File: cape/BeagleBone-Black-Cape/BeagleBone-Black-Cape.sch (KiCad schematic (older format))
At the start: 0 parts

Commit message: BBB cape rev-000
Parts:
- added J1, J2: USB_B, symbol USB_B
- added J3: Conn_01x03_Male, symbol Conn_01x03_Male
- added J4: Conn_01x02_Male, symbol Conn_01x02_Male
- added J5: Conn_01x05_Male, symbol Conn_01x05_Male
- added P8, P9: BeagleBone_Black_Header, symbol BeagleBone_Black_Header
- added U?: SN65HVD232, Housings_SOIC:SOIC-8_3.9x4.9mm_Pitch1.27mm, symbol SN65HVD232
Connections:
- new net +3V3: P9.3 (P3), P9.4 (P4), U?.3 (VCC)
- new net +5V: J1.1 (VBUS), J2.1 (VBUS), J3.3 (Pin_3), P9.5 (P5), P9.6 (P6)
- new net CANH: J4.1 (Pin_1), U?.7 (CANH)
- new net CANL: J4.2 (Pin_2), U?.6 (CANL)
- new net CAN_RX: U?.4 (R)
- new net CAN_TX: P9.24 (P24), U?.1 (D)
- new net GND: J1.4 (GND), J2.4 (GND), J3.1 (Pin_1), J5.5 (Pin_5), U?.2 (GND)
- new net GNDA_ADC: P9.34 (P34)
- new net GNDD: P8.1 (P1), P8.2 (P2), P9.1 (P1), P9.2 (P2), P9.43 (P43), P9.44 (P44), P9.45 (P45), P9.46 (P46)
- new net PWR_BUT: P9.9 (P9)
- new net SPI_MISO: J5.3 (Pin_3), P9.21 (P21)
- new net SPI_MOSI: J5.2 (Pin_2), P9.18 (P18)
- new net SPI_SCK: J5.4 (Pin_4), P9.22 (P22)
- new net SPI_SS: J5.1 (Pin_1), P9.17 (P17)
- new net SYS_5V: P9.7 (P7), P9.8 (P8)
- new net SYS_RESETN: P9.10 (P10)
- new net TACH_IN: J3.2 (Pin_2), P9.27 (P27)
- new net USB1+: J1.3 (D+), P8.15 (P15)
- new net USB1-: J1.2 (D-), P8.17 (P17)
- new net USB2+: J2.3 (D+), P8.16 (P16)
- new net USB2-: J2.2 (D-), P8.18 (P18)
- new net VDD_ADC: P9.32 (P32)
- no-connect marks 0 -> 2
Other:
- note added: "1. CANbus tranceiver has two sister chips that offer a \n offer "Standby" mode and "Sleep mode"\n2. Should we add any status LEDs for debug/functionality?\n3. Not sure if the shield option should be used for the USB.\n4. Bosch 928000453 for tachometer connection?\n"
- note added: "Notes:"
- note removed: "USB"
- note removed: "\n"

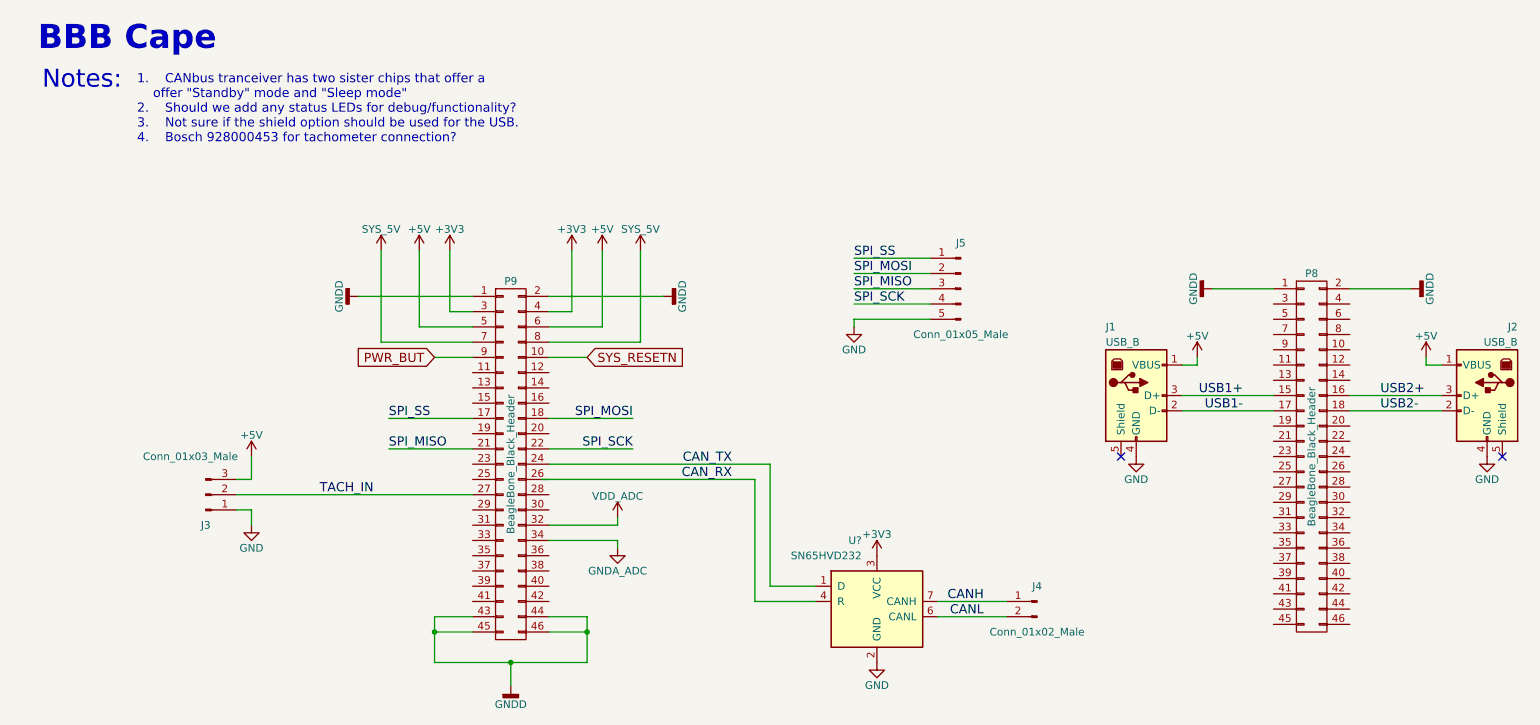
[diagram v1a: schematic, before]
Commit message: Updated cape schematic with the following: 1.) Pull-up resitors for SPI 2.) Grounded USB shield 3.) Changed SPI Connector to 2x3 header 4.) Added termination resistor to CANBUS driver
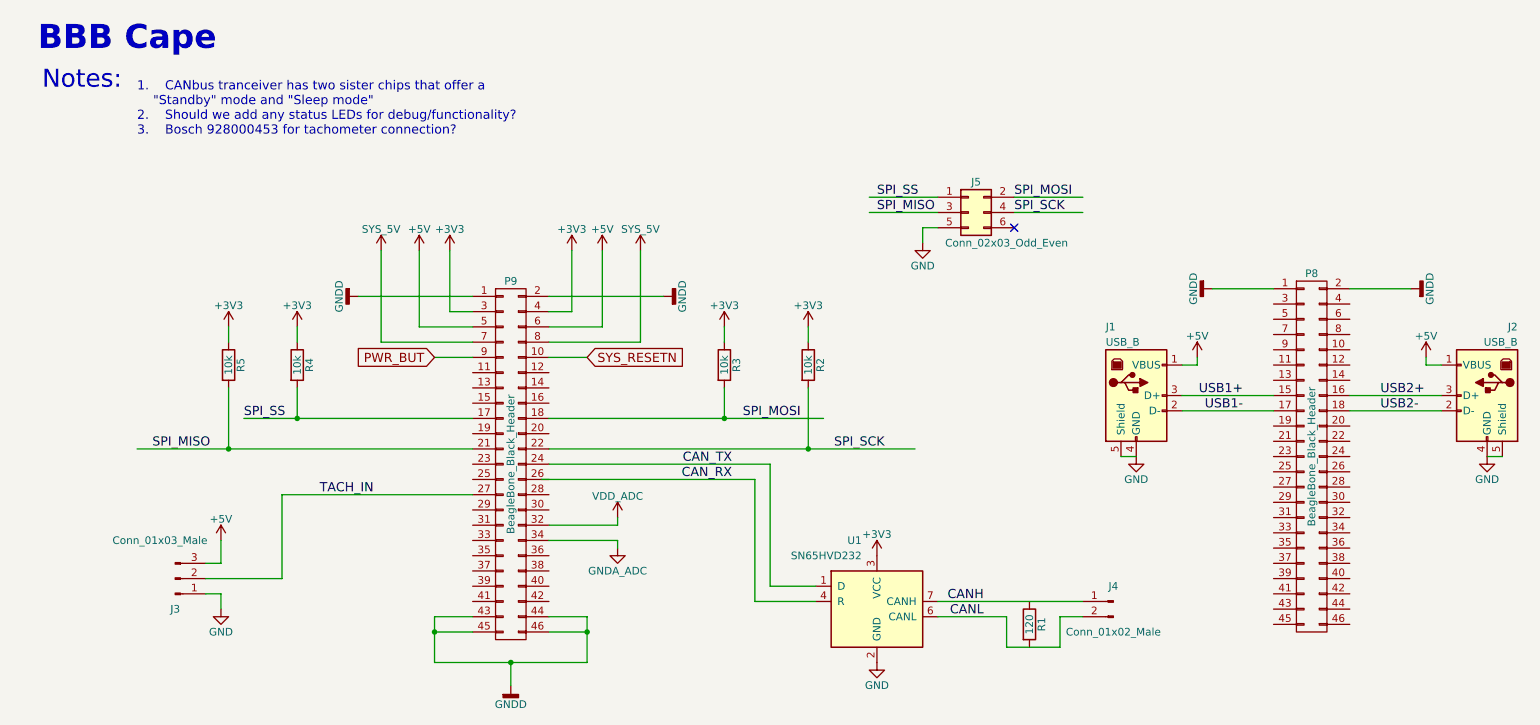
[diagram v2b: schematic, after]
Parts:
- removed J5: Conn_01x05_Male, symbol Conn_01x05_Male
- added J5: Conn_02x03_Odd_Even, symbol Conn_02x03_Odd_Even
- added R1: 120, symbol R
- added R2, R3, R4, R5: 10k, symbol R
- gave numbers to parts that had none: 1
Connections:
- wire segments 61 -> 77
- no-connect marks 2 -> 1
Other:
- note added: "1. CANbus tranceiver has two sister chips that offer a\n "Standby" mode and "Sleep mode"\n2. Should we add any status LEDs for debug/functionality?\n3. Bosch 928000453 for tachometer connection?\n"
- note removed: "1. CANbus tranceiver has two sister chips that offer a \n offer "Standby" mode and "Sleep mode"\n2. Should we add any status LEDs for debug/functionality?\n3. Not sure if the shield option should be used for the USB.\n4. Bosch 928000453 for tachometer connection?\n"
- moved on the sheet: J3, J4
